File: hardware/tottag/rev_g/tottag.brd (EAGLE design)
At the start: 68.1 x 39.5 mm, 199 parts, among them J1 USB4110-GF-A, J2 DM3AT-SF-PEJM5, J3 TC2030-JLINK-NL-2SIDE, J4 TC2030-JLINK-NL-2SIDE, J5 MOLEX-PICO-SPOX-3SIDE, Q1 CSD75207W15, Q4 CSD75207W15, T1 HHM1595A1, U1 DW1000, U10 STM32F091CC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

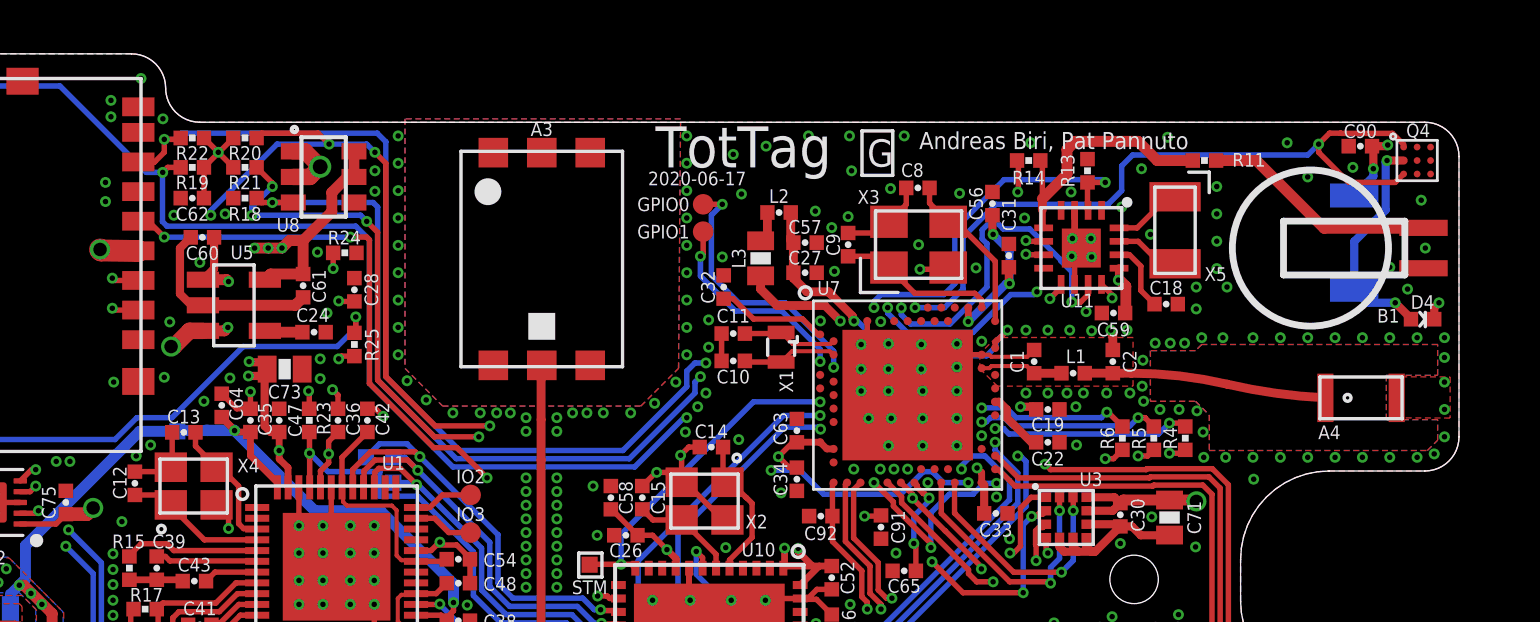
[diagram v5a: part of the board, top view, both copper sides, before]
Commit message: rev_g: [WIP] design review fixes
 - add missing keepouts for bottom-left antenna
 - improve (increase) power connections around speaker parts
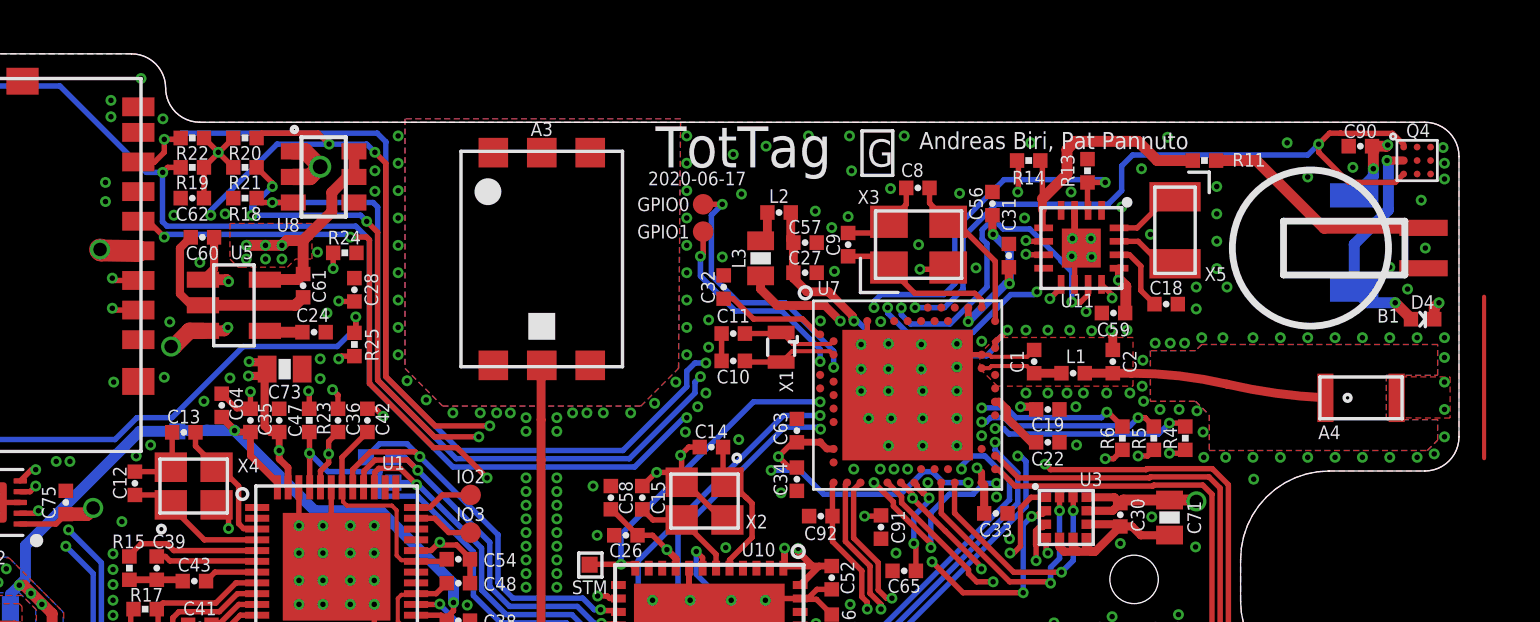
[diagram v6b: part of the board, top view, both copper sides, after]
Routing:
- net N$33: track 0.00 -> 6.00 mm
- net +3V3: track 146.6 -> 146.9 mm, vias 39 -> 42
- net GND: vias 529 -> 532
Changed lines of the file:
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@@
 <vertex x="-27.94" y="0.508"/>
 </polygon>
+<via x="33.528" y="28.3718" extent="1-16" drill="0.2032"/>
+<via x="33.528" y="28.956" extent="1-16" drill="0.2032"/>
+<via x="33.4772" y="29.5402" extent="1-16" drill="0.2032"/>
 </signal>
 <signal name="VUSB">
@@
 <wire x1="-7.112" y1="26.2128" x2="-6.5024" y2="26.2128" width="0.2032" layer="1"/>
 <wire x1="-6.5024" y1="26.2128" x2="-6.4008" y2="26.1112" width="0.2032" layer="1"/>
-<wire x1="-14.0208" y1="26.2128" x2="-7.112" y2="26.2128" width="0.2032" layer="16"/>
+<wire x1="-14.0208" y1="26.2128" x2="-13.9192" y2="26.3144" width="0.2032" layer="16"/>
+<wire x1="-7.2136" y1="26.3144" x2="-13.9192" y2="26.3144" width="0.2032" layer="16"/>
+<wire x1="-7.2136" y1="26.3144" x2="-7.112" y2="26.2128" width="0.2032" layer="16"/>
 <wire x1="-6.4008" y1="20.7786875" x2="-6.4008" y2="26.1112" width="0.2032" layer="1"/>
 <via x="13.7708625" y="16.5140625" extent="1-16" drill="0.2032"/>
@@
 <contactref element="C90" pad="1"/>
 <wire x1="30.83686875" y1="29.591" x2="30.8864" y2="29.54146875" width="0.254" layer="1"/>
-<wire x1="30.8864" y1="29.54146875" x2="30.8864" y2="28.7528" width="0.3048" layer="1"/>
+<wire x1="30.8864" y1="29.54146875" x2="30.8864" y2="28.7528" width="0.4064" layer="1"/>
 <via x="30.8864" y="28.7528" extent="1-16" drill="0.2032"/>
 <wire x1="-20.5486" y1="12.2428" x2="-20.5486" y2="12.1666" width="0.4064" layer="16"/>
@@
 <contactref element="LS1" pad="+"/>
 <contactref element="D4" pad="CATHODE"/>
-<wire x1="30.1752" y1="27.7596" x2="30.8864" y2="28.4708" width="0.3048" layer="16"/>
-<wire x1="30.8864" y1="28.4708" x2="30.8864" y2="28.7528" width="0.3048" layer="16"/>
-<wire x1="33.14826875" y1="23.1648" x2="33.14826875" y2="23.59786875" width="0.3048" layer="1"/>
-<wire x1="33.14826875" y1="23.59786875" x2="33.3248" y2="23.7744" width="0.3048" layer="1"/>
+<wire x1="30.1752" y1="27.7596" x2="30.8864" y2="28.4708" width="0.4064" layer="16"/>
+<wire x1="30.8864" y1="28.4708" x2="30.8864" y2="28.7528" width="0.4064" layer="16"/>
+<wire x1="33.14826875" y1="23.1648" x2="33.14826875" y2="23.59786875" width="0.4064" layer="1"/>
+<wire x1="33.14826875" y1="23.59786875" x2="33.3248" y2="23.7744" width="0.4064" layer="1"/>
 <via x="33.3248" y="23.7744" extent="1-16" drill="0.2032"/>
 <wire x1="-21.3337" y1="9.9402" x2="-21.44536875" y2="9.82853125" width="0.4064" layer="1"/>
@@
 <wire x1="29.7942" y1="0.5842" x2="29.464" y2="0.9144" width="0.2032" layer="16"/>
 <wire x1="29.464" y1="0.9144" x2="28.2448" y2="0.9144" width="0.2032" layer="16"/>
-<wire x1="-10.28450625" y1="24.63134375" x2="-10.07338125" y2="24.84246875" width="0.4064" layer="1"/>
-<wire x1="-10.07338125" y1="24.84246875" x2="-8.8646" y2="24.84246875" width="0.4064" layer="1"/>
+<wire x1="-10.28450625" y1="24.63134375" x2="-10.27658125" y2="24.63926875" width="0.4064" layer="1"/>
+<wire x1="-9.0678" y1="24.63926875" x2="-10.27658125" y2="24.63926875" width="0.4064" layer="1"/>
+<wire x1="-9.0678" y1="24.63926875" x2="-8.8646" y2="24.84246875" width="0.4064" layer="1"/>
 <wire x1="-8.8646" y1="24.84246875" x2="-8.8646" y2="26.0858" width="0.4064" layer="1"/>
 <wire x1="-8.8646" y1="26.0858" x2="-7.7978" y2="27.1526" width="0.4064" layer="1"/>
-<wire x1="-8.8646" y1="26.0858" x2="-9.3726" y2="26.0858" width="0.4064" layer="1"/>
-<wire x1="-9.3726" y1="26.0858" x2="-9.652" y2="25.8064" width="0.4064" layer="1"/>
-<via x="-9.652" y="25.8064" extent="1-16" drill="0.2032"/>
-<wire x1="-9.652" y1="25.8064" x2="-10.16" y2="25.8064" width="0.4064" layer="1"/>
-<via x="-10.16" y="25.8064" extent="1-16" drill="0.2032"/>
-<wire x1="-10.16" y1="25.8064" x2="-10.668" y2="25.8064" width="0.4064" layer="1"/>
-<via x="-10.668" y="25.8064" extent="1-16" drill="0.2032"/>
-<wire x1="33.3248" y1="23.7744" x2="33.3248" y2="27.8384" width="0.3048" layer="15"/>
-<wire x1="33.3248" y1="27.8384" x2="32.7152" y2="28.448" width="0.3048" layer="15"/>
-<wire x1="32.7152" y1="28.448" x2="31.1912" y2="28.448" width="0.3048" layer="15"/>
-<wire x1="31.1912" y1="28.448" x2="30.8864" y2="28.7528" width="0.3048" layer="15"/>
-<wire x1="30.83686875" y1="29.591" x2="31.37535" y2="29.591" width="0.3048" layer="1"/>
-<wire x1="31.37535" y1="29.591" x2="31.4198" y2="29.63545" width="0.3048" layer="1"/>
+<wire x1="-8.8646" y1="26.0858" x2="-9.4742" y2="26.0858" width="0.4064" layer="1"/>
+<wire x1="-9.4742" y1="26.0858" x2="-9.652" y2="25.908" width="0.4064" layer="1"/>
+<via x="-9.652" y="25.908" extent="1-16" drill="0.2032"/>
+<wire x1="-9.652" y1="25.908" x2="-10.2616" y2="25.908" width="0.4064" layer="1"/>
+<via x="-10.2616" y="25.908" extent="1-16" drill="0.2032"/>
+<wire x1="-10.2616" y1="25.908" x2="-10.9728" y2="25.908" width="0.4064" layer="1"/>
+<via x="-10.9728" y="25.908" extent="1-16" drill="0.2032"/>
+<wire x1="33.3248" y1="23.7744" x2="33.3248" y2="27.8384" width="0.4064" layer="15"/>
+<wire x1="33.3248" y1="27.8384" x2="32.7152" y2="28.448" width="0.4064" layer="15"/>
+<wire x1="32.7152" y1="28.448" x2="31.1912" y2="28.448" width="0.4064" layer="15"/>
+<wire x1="31.1912" y1="28.448" x2="30.8864" y2="28.7528" width="0.4064" layer="15"/>
+<wire x1="30.83686875" y1="29.591" x2="31.37535" y2="29.591" width="0.4064" layer="1"/>
+<wire x1="31.37535" y1="29.591" x2="31.4198" y2="29.63545" width="0.4064" layer="1"/>
 <via x="31.4198" y="29.63545" extent="1-16" drill="0.2032"/>
-<wire x1="31.4198" y1="29.63545" x2="29.63545" y2="29.63545" width="0.3048" layer="15"/>
-<wire x1="29.63545" y1="29.63545" x2="28.448" y2="28.448" width="0.3048" layer="15"/>
+<wire x1="31.4198" y1="29.63545" x2="29.63545" y2="29.63545" width="0.4064" layer="15"/>
+<wire x1="29.63545" y1="29.63545" x2="28.448" y2="28.448" width="0.4064" layer="15"/>
 <via x="28.448" y="28.448" extent="1-16" drill="0.2032"/>
 <wire x1="2.5654" y1="16.10233125" x2="2.5933375" y2="16.10233125" width="0.2032" layer="1"/>
@@
 <vertex x="-23.3426" y="10.287"/>
 </polygon>
+<polygon width="0.0508" layer="1" thermals="no">
+<vertex x="-11.5824" y="26.416"/>
+<vertex x="-11.5824" y="25.4"/>
+<vertex x="-11.2776" y="25.0952"/>
+<vertex x="-11.176" y="25.0952"/>
+<vertex x="-9.4488" y="25.0952"/>
+<vertex x="-9.144" y="25.4"/>
+<vertex x="-8.5344" y="25.4"/>
+<vertex x="-8.5344" y="26.7208"/>
+<vertex x="-11.5824" y="26.7208"/>
+</polygon>
+<via x="-10.9728" y="25.4" extent="1-16" drill="0.2032"/>
+<via x="-10.2616" y="25.4" extent="1-16" drill="0.2032"/>
+<via x="-9.652" y="25.4" extent="1-16" drill="0.2032"/>
 </signal>
 <signal name="N$22">
@@
 <contactref element="D4" pad="ANODE"/>
 <via x="31.3944" y="29.0576" extent="1-16" drill="0.2032"/>
-<wire x1="31.3436" y1="29.0068" x2="31.3944" y2="29.0576" width="0.3048" layer="16"/>
-<wire x1="30.1752" y1="26.0503875" x2="31.3436" y2="27.2187875" width="0.3048" layer="16"/>
-<wire x1="31.3436" y1="27.2187875" x2="31.3436" y2="29.0068" width="0.3048" layer="16"/>
+<wire x1="30.1752" y1="25.9487875" x2="31.4452" y2="27.2187875" width="0.4064" layer="16"/>
+<wire x1="31.3944" y1="29.0576" x2="31.4452" y2="29.0068" width="0.4064" layer="16"/>
+<wire x1="31.4452" y1="29.0068" x2="31.4452" y2="27.2187875" width="0.4064" layer="16"/>
 <wire x1="31.3944" y1="29.0576" x2="32.012" y2="29.0576" width="0.3048" layer="1"/>
-<wire x1="30.1752" y1="24.2596" x2="30.1752" y2="26.0503875" width="0.3048" layer="16"/>
-<wire x1="30.1752" y1="24.2596" x2="30.6604" y2="23.7744" width="0.3048" layer="16"/>
-<wire x1="30.6604" y1="23.7744" x2="31.6992" y2="23.7744" width="0.3048" layer="16"/>
+<wire x1="30.1752" y1="24.2596" x2="30.1752" y2="25.9487875" width="0.4064" layer="16"/>
+<wire x1="30.1752" y1="24.2596" x2="30.6604" y2="23.7744" width="0.4064" layer="16"/>
+<wire x1="30.6604" y1="23.7744" x2="31.6992" y2="23.7744" width="0.4064" layer="16"/>
 <via x="31.6992" y="23.7744" extent="1-16" drill="0.2032"/>
-<wire x1="31.6992" y1="23.7744" x2="32.28213125" y2="23.19146875" width="0.3048" layer="1"/>
+<wire x1="31.6992" y1="23.7744" x2="32.28213125" y2="23.19146875" width="0.4064" layer="1"/>
 <wire x1="32.28213125" y1="23.19146875" x2="32.28213125" y2="23.1648" width="0.3048" layer="1"/>
 </signal>
@@
 <wire x1="14.8336" y1="-5.86866875" x2="13.6144" y2="-5.86866875" width="0.1524" layer="1"/>
 </signal>
+<signal name="N$33">
+<wire x1="35" y1="18" x2="35" y2="24" width="0.1524" layer="1"/>
+</signal>
 </signals>

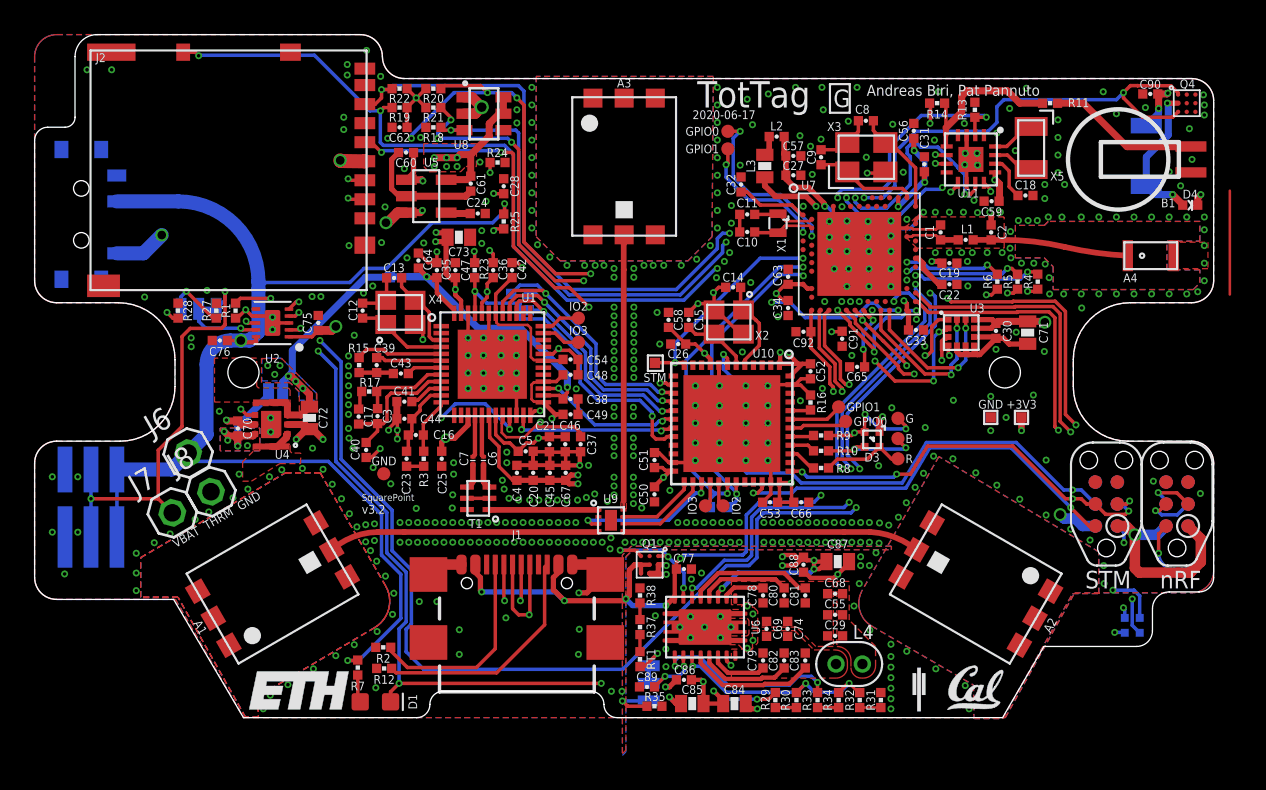
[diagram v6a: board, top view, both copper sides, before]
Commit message: rev_g: [WIP] Update BLE Antenna layout
 - Unsure about weird ground stub on reference drawing
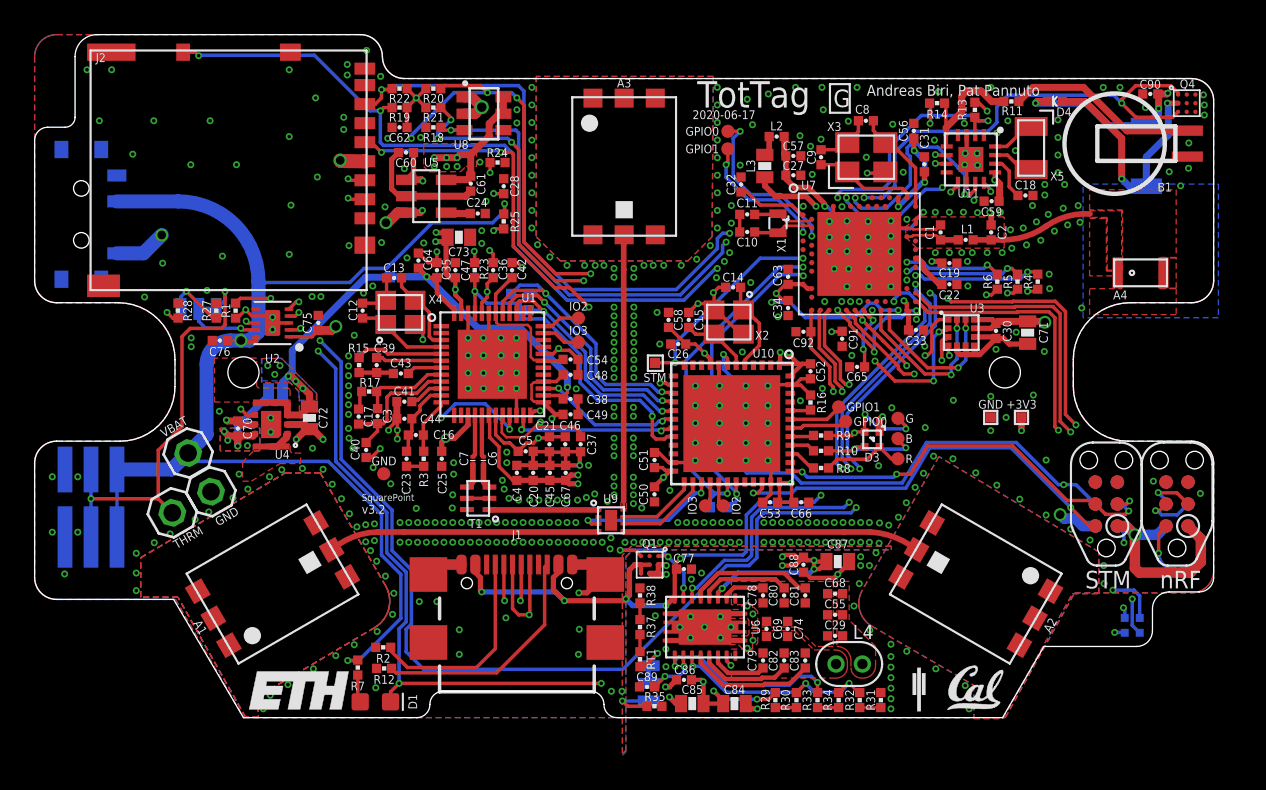
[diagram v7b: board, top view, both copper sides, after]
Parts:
- moved D4 9.86 mm to (24.9, 29.2), turned to 180 degrees
- moved R11 2.24 mm to (22.4, 29.2)
- moved A4 1.15 mm to (29.8, 19.3)
- moved B1 0.94 mm to (28.3, 26.7)
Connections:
- net N$17 renamed BLE_ANT
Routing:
- net N$33: track 6.00 -> 0.00 mm
- net N$2: track 8.54 -> 14.2 mm
- net N$45: track 8.75 -> 11.1 mm
- net VBAT_RTC: track 9.85 -> 7.58 mm
- net BLE_ANT: track 8.99 -> 6.97 mm
- net GND: track 158.5 -> 159.4 mm, vias 532 -> 528
- net !STM_RST: track 35.7 -> 36.3 mm
- net STM_SWDCLK: vias 4 -> 3
- added copper zone on layer 2, net +3V3
- added copper zone on layer 1, net BLE_ANT
- added copper zone on layer 2, net N$31
- removed copper zone on layer 1, net N$46
- removed copper zone on layer 15, net N$46
- removed copper zone on layer 16, net N$46
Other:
- board text added: "0.3"
- board text added: "0.74"
- board text added: "0.85"
- board text added: "0.95"
- board text added: "1.0"
- board text added: "1.22"
- board text added: "1.8"
- board text added: "1.85"
- board text added: "3.42"
- board text added: "5.0"
- board text added: "6.0"
- board text added: "???"
- board text added: "THRM"
- board text added: "VBAT"
- board text removed: "GND THRM VBAT"
- board text removed: "VBAT THRM GND"

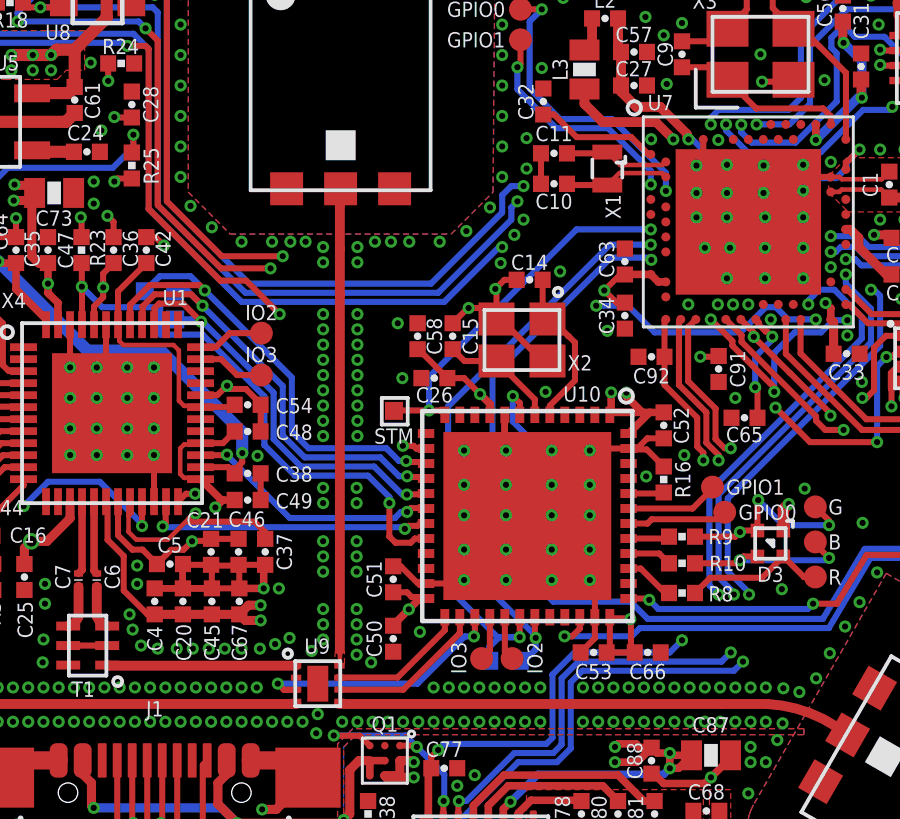
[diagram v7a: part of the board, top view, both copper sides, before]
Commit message: rev_g: Move the nrf escape to improve gnd layer
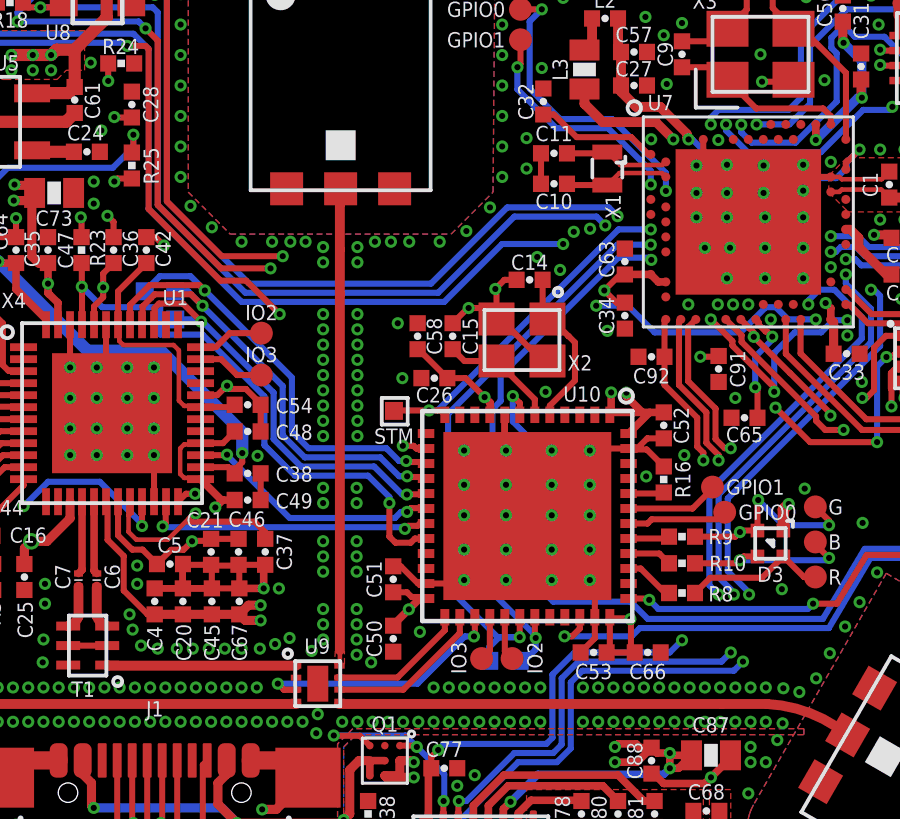
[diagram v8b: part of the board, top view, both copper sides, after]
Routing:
- net STM_INTERRUPT: track 12.3 -> 11.7 mm
